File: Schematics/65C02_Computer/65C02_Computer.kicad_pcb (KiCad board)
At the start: 2 copper layers, 203.2 x 149.9 mm, 60 parts, among them J1 CLK Jumper, J2 Expansion port, J3 USB_B_Micro, J4 LCD Connector, J5 VIA2PA, J6 VIA2PB, J7 Mini-DIN-6, SW1 RESET, U1 74HC02, U10 FT230XS, U11 65C51N, U12 ATtiny4313-PU, U2 28C256, U3 65C02S, U4 74HC00, U5 74HC21, U6 62256, U7 NE555, U8 65C22S, U9 65C22S, X1 1MHz, X2 1.8432MHz

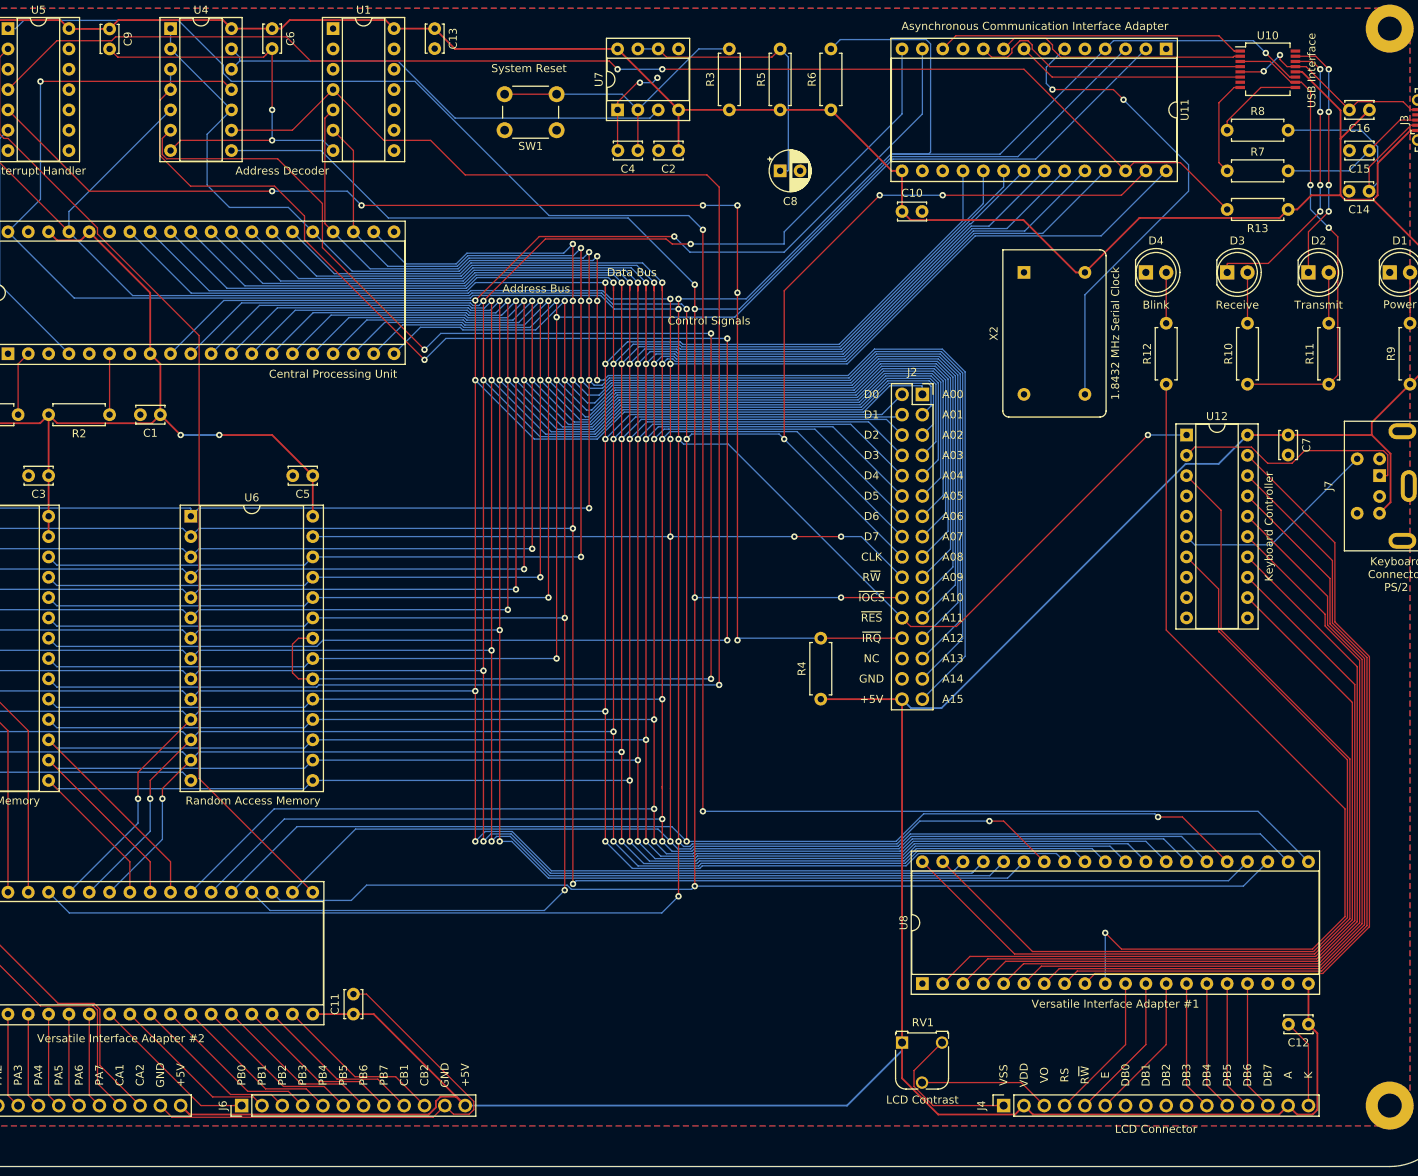
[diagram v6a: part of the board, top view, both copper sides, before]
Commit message: Moved VIA1
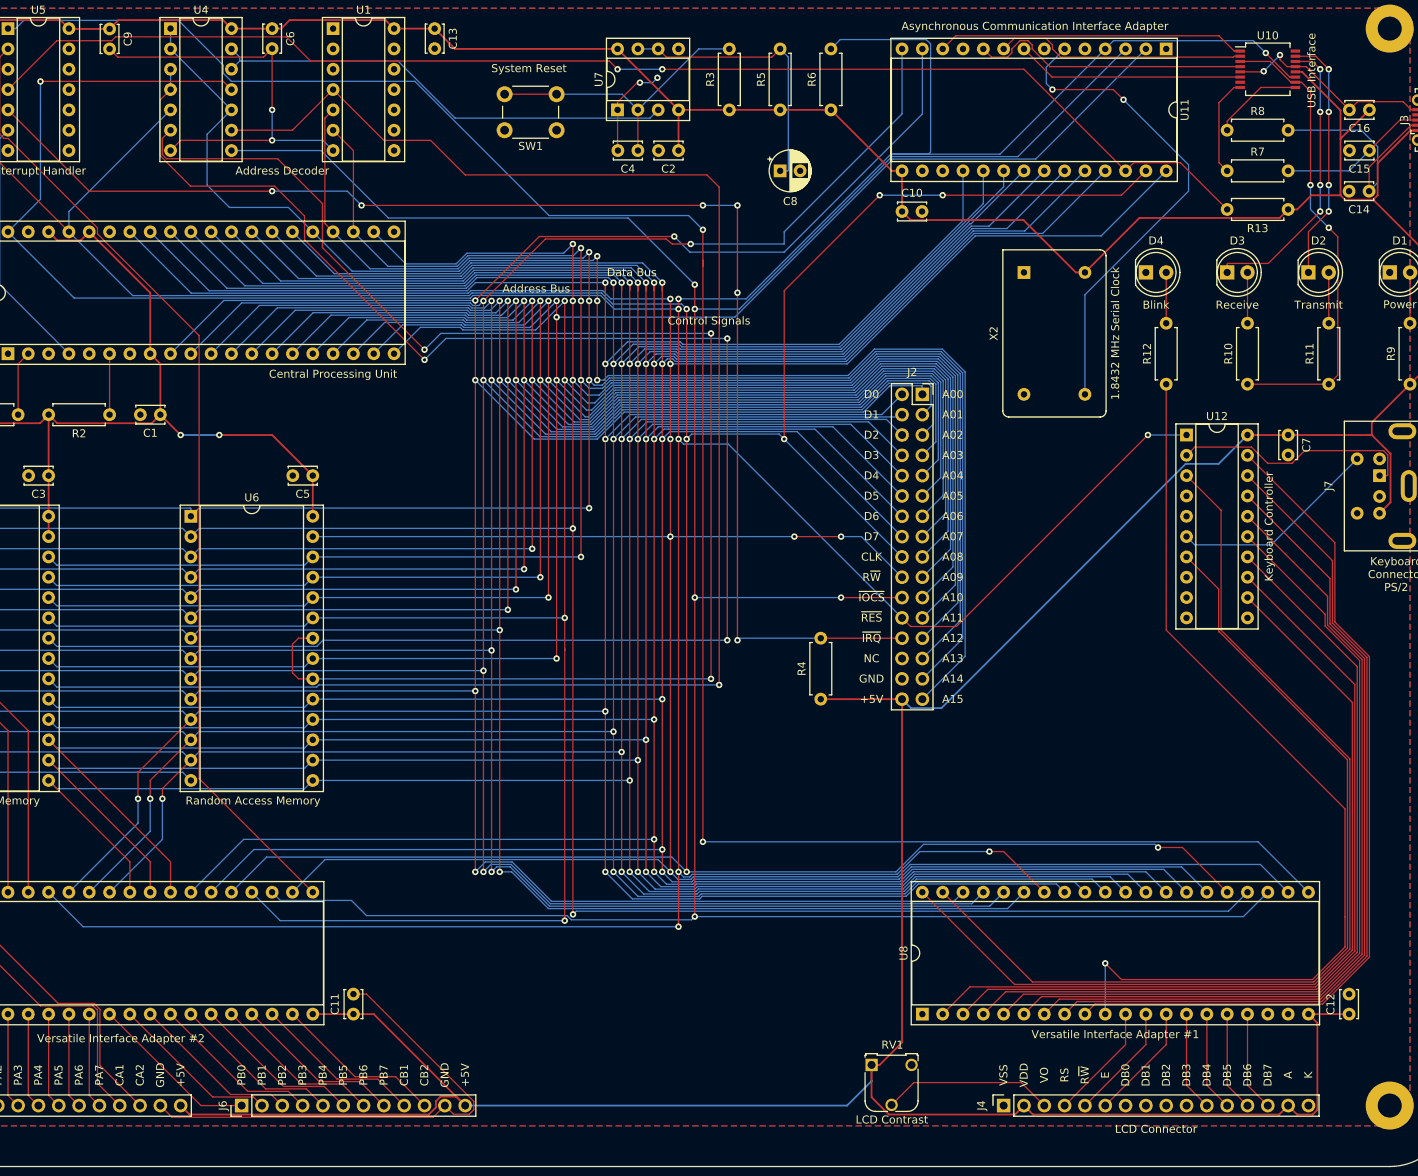
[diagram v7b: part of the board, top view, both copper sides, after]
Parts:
- moved C12 5.24 mm to (208.3, 151.1), turned to 90 degrees
- moved RV1 4.72 mm to (148.6, 157.5)
- moved U8 3.81 mm to (154.9, 151.1)
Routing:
- net GND: track 220.3 -> 190.0 mm
- net Net-(J4-Pad3): track 16.5 -> 21.4 mm
- net ~V1IRQ: track 249.7 -> 254.3 mm
- net +5V: track 767.8 -> 772.1 mm
- net /6502 Peripherals/v1pb0: track 114.7 -> 118.5 mm
- net a3: track 352.8 -> 356.6 mm
- net a1: track 410.9 -> 414.7 mm
- net /6502 Peripherals/v1pa9: track 110.5 -> 114.3 mm
- net /6502 Peripherals/v1pb3: track 18.4 -> 14.6 mm
- net d5: track 391.2 -> 395.0 mm
- net d4: track 385.3 -> 389.1 mm
- net d2: track 396.4 -> 400.2 mm
- net a12: track 361.7 -> 365.5 mm
- net a0: track 406.6 -> 410.4 mm
- net /6502 Peripherals/v1pb7: track 16.3 -> 12.5 mm
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
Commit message: Small changes
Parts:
- added REF**: KiCad-Logo2_8mm_SilkScreen, Symbol:KiCad-Logo2_8mm_SilkScreen, F.Cu at (172.7, 119.4)
- added REF**: OSHW-Logo_11.4x12mm_SilkScreen, Symbol:OSHW-Logo_11.4x12mm_SilkScreen, F.Cu at (191.8, 120.7)
- U10: footprint Package_SO:SSOP-16_5.3x6.2mm_P0.65mm -> Package_SO:SSOP-16_4.4x5.2mm_P0.65mm
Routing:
- net GND: track 190.0 -> 186.5 mm, vias 6 -> 5
- net +5V: track 772.1 -> 772.6 mm
- net Net-(R10-Pad1): track 59.0 -> 58.4 mm
- net ~RTS: track 28.5 -> 29.0 mm
- net ~CTS: track 31.4 -> 32.0 mm
- net USBD+: track 12.4 -> 12.9 mm
- net RxD: track 38.7 -> 39.2 mm
- net TxD: track 35.3 -> 35.9 mm
- net USBD-: track 11.4 -> 10.9 mm
- net Net-(D3-Pad1): track 36.7 -> 37.2 mm
- net Net-(D2-Pad1): track 31.3 -> 31.8 mm
- net ~RES: track 548.5 -> 548.0 mm
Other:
- board text added: "Author: Dawid Buchwald"
- board text added: "Based on Ben Eater’s 6502 project"
- board text added: "Board revision: v001"
- board text added: "VIA 2 Port A"
- board text added: "VIA 2 Port B"
- board text added: "https://github.com/dbuchwald/6502"
